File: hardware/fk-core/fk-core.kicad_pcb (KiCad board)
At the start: 2 copper layers, 26.2 x 105.4 mm, 72 parts, among them J1 S2B-PH-SM4-TB, J2 MICRO-USB, J3 RF-SMA-EDGE, J4 CONN-HDR-1x19, J5 CONN-HDR-1x19, J6 CONN-HDR-2x5, J7 RF-SMA-EDGE, M1 MOUNT_HOLE, M2 MOUNT_HOLE, M3 MOUNT_HOLE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

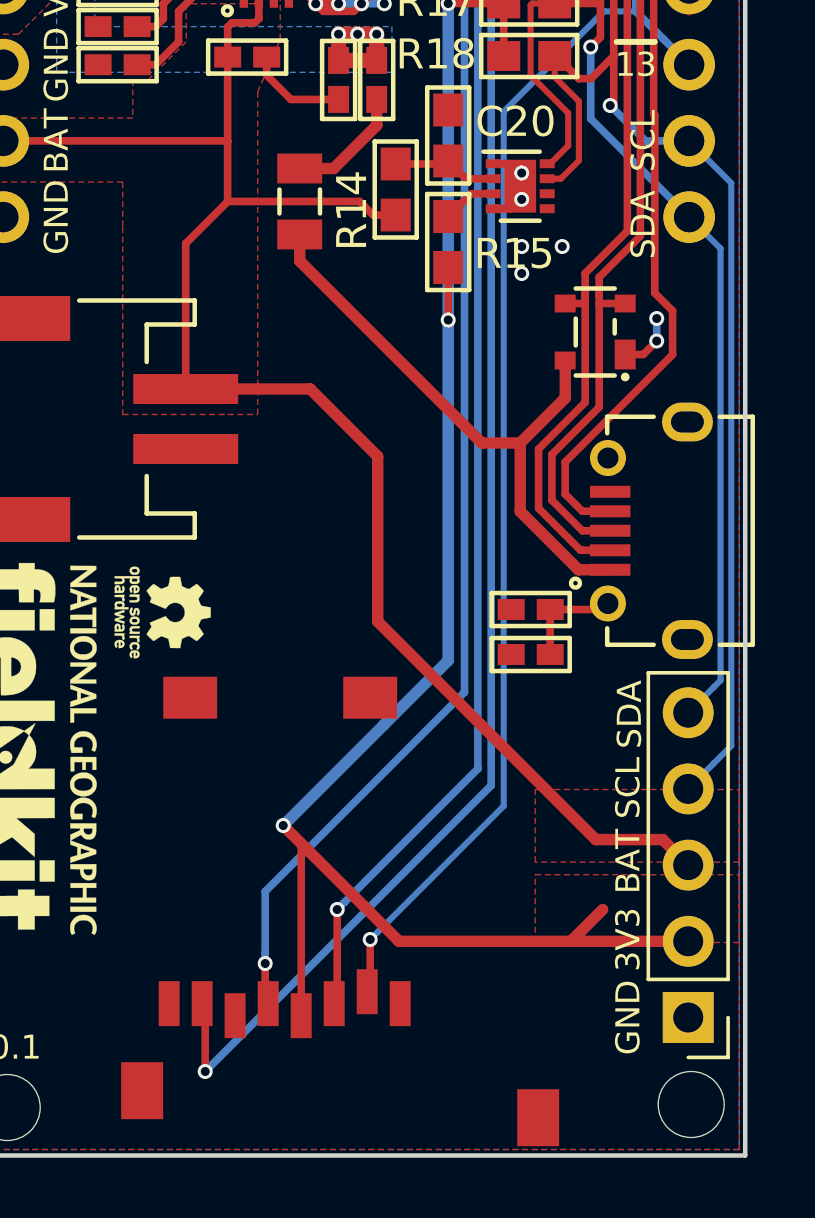
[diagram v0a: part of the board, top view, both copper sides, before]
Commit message: Nudge periph header down to clear USB.
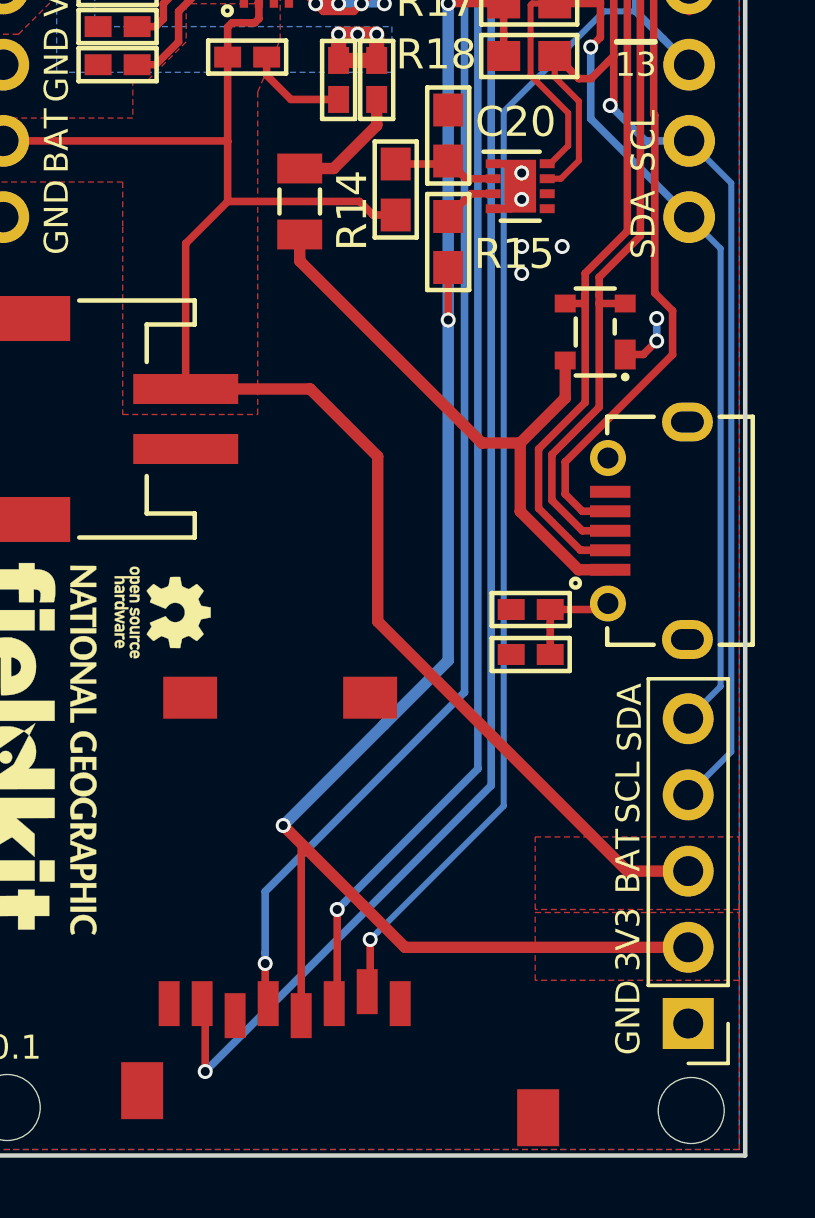
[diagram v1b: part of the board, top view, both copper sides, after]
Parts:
- moved P1 0.20 mm to (151.1, 148.8)
- moved M2 0.20 mm to (151.2, 151.7)
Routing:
- net 3V3: track 209.9 -> 208.4 mm
